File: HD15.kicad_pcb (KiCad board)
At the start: 2 copper layers, 110 x 62 mm, 46 parts, among them CN1 9, CN2 9, CN3 35RAPC4BH3, CN5 B6B-XH-A(LF)(SN), CN6 353180620, J1A JAMMA PINS 3.96MM PITCH 2.2MM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, J1B JAMMA PINS 3.96MM PITCH 2.2MM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, SW1 MJTP1230, SW2 MJTP1230, SW3 DIPSwitch-4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

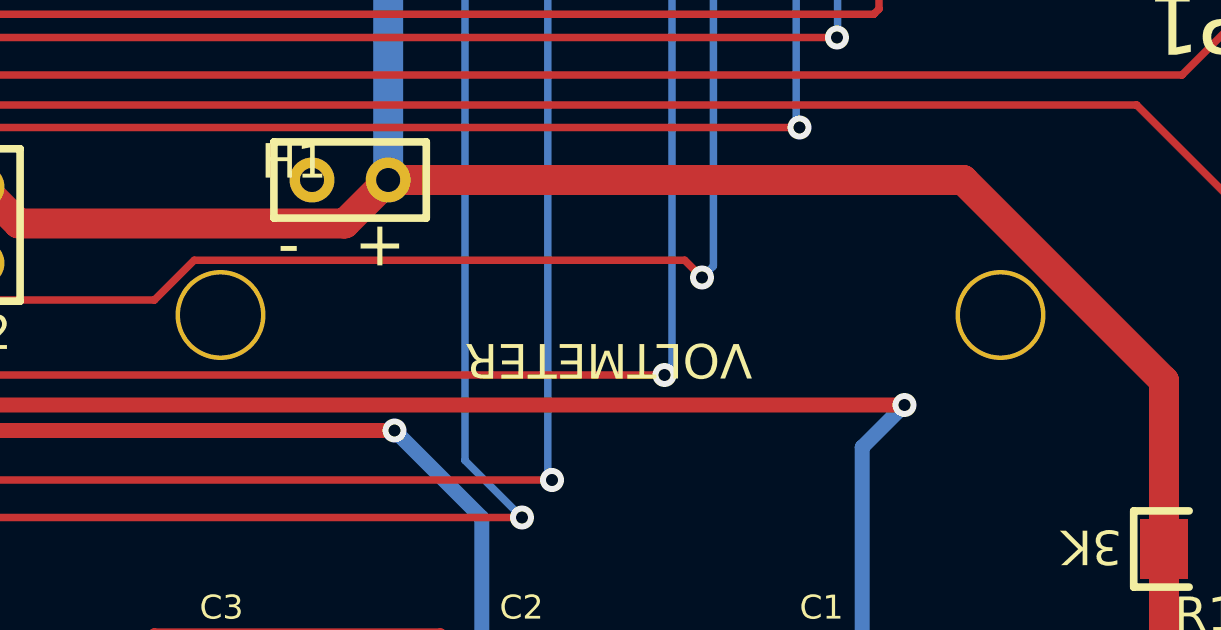
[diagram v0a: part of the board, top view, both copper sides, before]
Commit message: Mounting holes down to 2.0mm
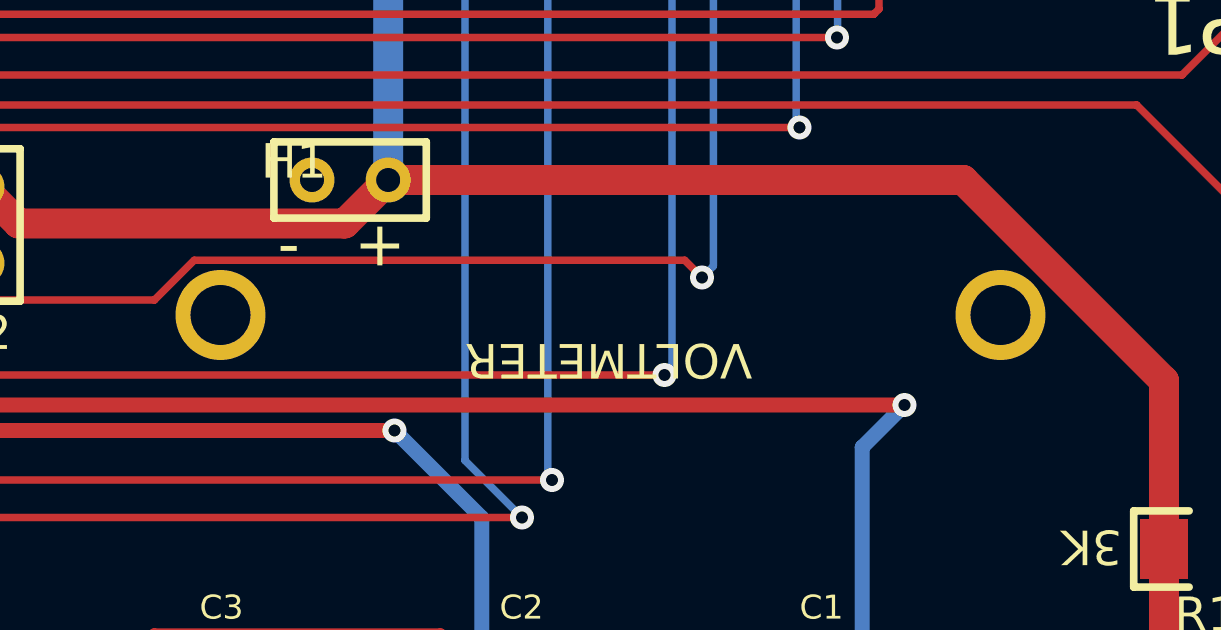
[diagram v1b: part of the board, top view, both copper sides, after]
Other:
- board text added: "REV_2.5+HD15_0.3"
- board text removed: "REV_2.5+HD15_0.2"
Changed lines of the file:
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@@
   )
   (setup
-    (last_trace_width 1)
+    (last_trace_width 0.25)
     (user_trace_width 0.38)
     (user_trace_width 0.5)
@@
     (mod_text_size 1 1)
     (mod_text_width 0.15)
-    (pad_size 1.651 1.651)
-    (pad_drill 1.143)
+    (pad_size 3 3)
+    (pad_drill 2)
     (pad_to_mask_clearance 0)
     (aux_axis_origin 0 0)
@@
       (effects (font (size 1 1) (thickness 0.15)))
     )
-    (pad "" np_thru_hole circle (at -13 0) (size 3 3) (drill 2.7) (layers *.Cu *.Mask))
-    (pad "" np_thru_hole circle (at 13 0) (size 3 3) (drill 2.7) (layers *.Cu *.Mask))
+    (pad "" np_thru_hole circle (at -13 0) (size 3 3) (drill 2) (layers *.Cu *.Mask))
+    (pad "" np_thru_hole circle (at 13 0) (size 3 3) (drill 2) (layers *.Cu *.Mask))
   )
   (module "easyeda:3 PIN HEADER" (layer F.Cu)
@@
     (effects (font (size 1 1) (thickness 0.15)) (justify mirror))
   )
-  (gr_text REV_2.5+HD15_0.2 (at 108.654 29.5) (layer B.SilkS)
+  (gr_text REV_2.5+HD15_0.3 (at 108.654 29.5) (layer B.SilkS)
     (effects (font (size 1.5 1.5) (thickness 0.2)) (justify left mirror))
   )
@@
   (segment (start 51 17) (end 49.799991 15.799991) (width 0.5) (layer B.Cu) (net 4))
   (via (at 49.799991 9.799991) (size 0.8) (drill 0.4) (layers F.Cu B.Cu) (net 4))
-  (segment (start 36.910002 17.25) (end 36.5 17.25) (width 0.5) (layer B.Cu) (net 66))
   (via (at 75.25 -19.5) (size 0.8) (drill 0.4) (layers F.Cu B.Cu) (net 5))
   (segment (start 75.24 -19.49) (end 75.25 -19.5) (width 0.25) (layer B.Cu) (net 5))
@@
   (segment (start 39.4 20.65) (end 39.286411 20.65) (width 0.25) (layer F.Cu) (net 38))
   (segment (start 47.104 20.65) (end 39.4 20.65) (width 0.25) (layer F.Cu) (net 38))
-  (segment (start 19.495012 11.029988) (end 17.025 13.5) (width 0.38) (layer F.Cu) (net 66))
   (segment (start 39.4 20.65) (end 37.9 20.65) (width 0.38) (layer F.Cu) (net 38))
-  (segment (start 27.279988 11.029988) (end 19.495012 11.029988) (width 0.38) (layer F.Cu) (net 66))
   (segment (start 37.9 20.65) (end 36.5 19.25) (width 0.38) (layer F.Cu) (net 38))
   (segment (start 47.104 20.65) (end 37.9 20.65) (width 0.38) (layer F.Cu) (net 38))
@@
   (segment (start 54.1765 21.3) (end 52.895 21.3) (width 0.38) (layer F.Cu) (net 45))
   (segment (start 54.266502 21.209998) (end 54.1765 21.3) (width 0.38) (layer F.Cu) (net 45))
-  (segment (start 29 13.897998) (end 26.712001 11.609999) (width 0.38) (layer F.Cu) (net 64))
-  (segment (start 21.165001 11.609999) (end 17.025 15.75) (width 0.38) (layer F.Cu) (net 64))
-  (segment (start 26.712001 11.609999) (end 21.165001 11.609999) (width 0.38) (layer F.Cu) (net 64))
   (segment (start 39.3 22.2) (end 36.5 25) (width 0.38) (layer F.Cu) (net 46))
-  (segment (start 32.5 17.397998) (end 29 13.897998) (width 0.38) (layer F.Cu) (net 64))
   (segment (start 40.2 21.3) (end 36.5 25) (width 0.38) (layer F.Cu) (net 46))
   (segment (start 47.104 21.3) (end 40.2 21.3) (width 0.38) (layer F.Cu) (net 46))
@@
   (segment (start 6.5 33.25) (end 7.975002 31.774998) (width 0.25) (layer B.Cu) (net 63))
   (segment (start 10.75 32.684315) (end 10.75 33.25) (width 0.25) (layer B.Cu) (net 63))
+  (segment (start 29 13.897998) (end 26.712001 11.609999) (width 0.38) (layer F.Cu) (net 64))
+  (segment (start 21.165001 11.609999) (end 17.025 15.75) (width 0.38) (layer F.Cu) (net 64))
+  (segment (start 26.712001 11.609999) (end 21.165001 11.609999) (width 0.38) (layer F.Cu) (net 64))
+  (segment (start 32.5 17.397998) (end 29 13.897998) (width 0.38) (layer F.Cu) (net 64))
   (segment (start 32.5 19) (end 36.5 23) (width 0.38) (layer F.Cu) (net 64))
   (segment (start 32.5 17.397998) (end 32.5 19) (width 0.38) (layer F.Cu) (net 64))
@@
   (segment (start 36.5 11.5) (end 29.43002 11.5) (width 0.38) (layer F.Cu) (net 65))
   (segment (start 18.24001 10.03499) (end 27.96501 10.03499) (width 0.38) (layer F.Cu) (net 65))
+  (segment (start 36.910002 17.25) (end 36.5 17.25) (width 0.5) (layer B.Cu) (net 66))
+  (segment (start 19.495012 11.029988) (end 17.025 13.5) (width 0.38) (layer F.Cu) (net 66))
+  (segment (start 27.279988 11.029988) (end 19.495012 11.029988) (width 0.38) (layer F.Cu) (net 66))
   (segment (start 33.5 17.25) (end 27.279988 11.029988) (width 0.38) (layer F.Cu) (net 66))
   (segment (start 36.5 17.25) (end 33.5 17.25) (width 0.38) (layer F.Cu) (net 66))

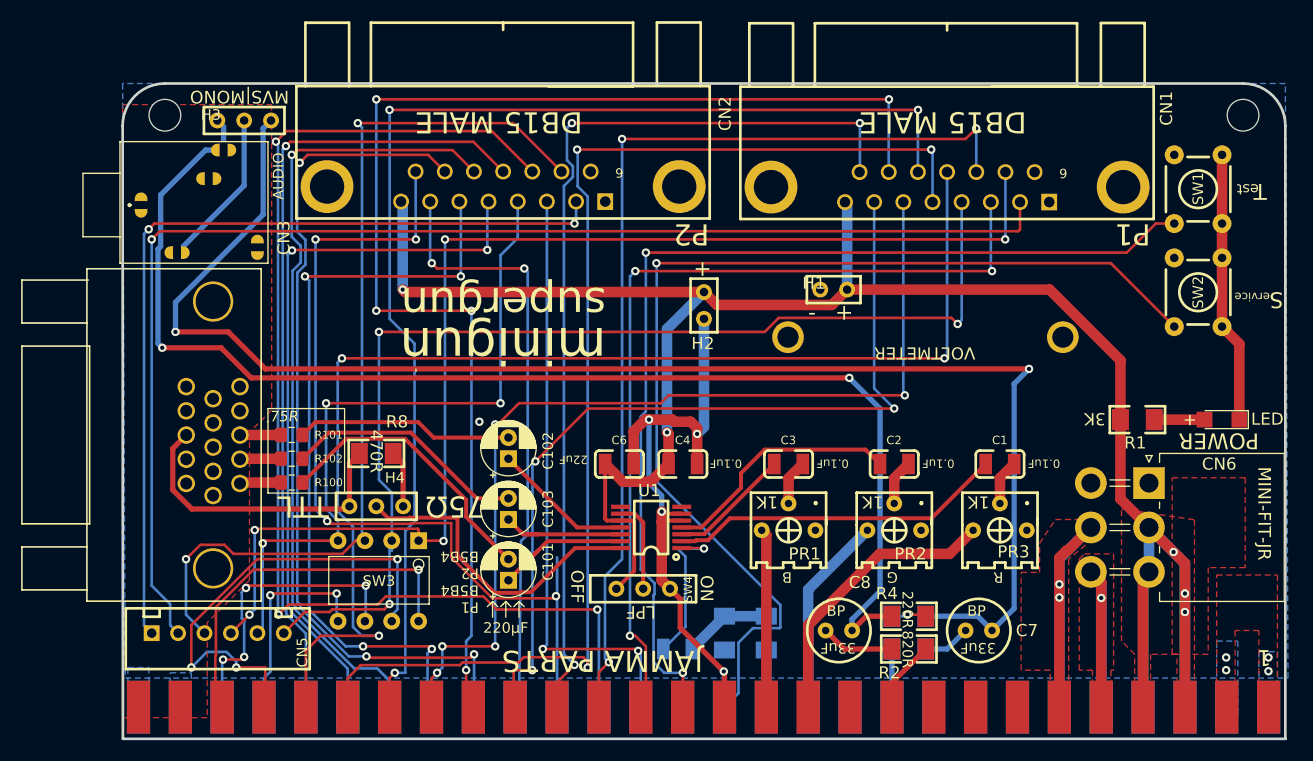
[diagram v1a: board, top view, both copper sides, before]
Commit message: Convert to KiCad 6
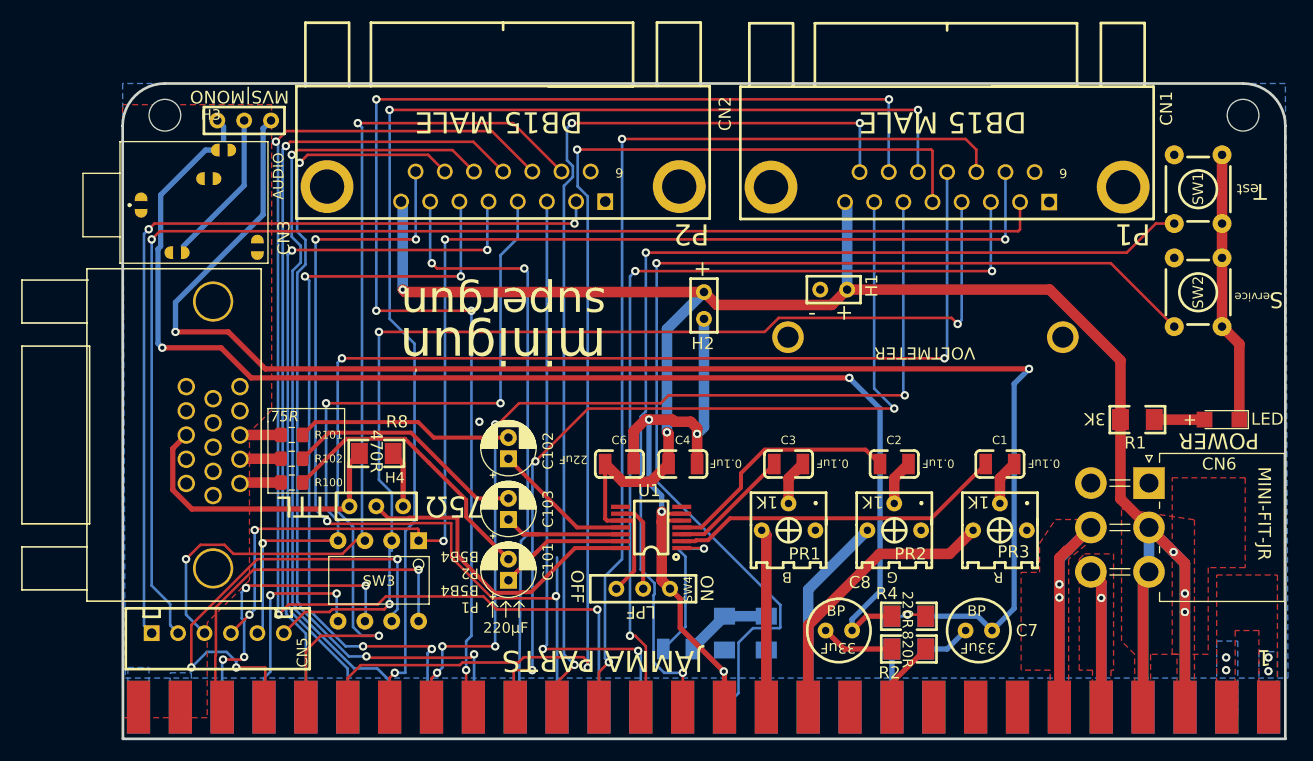
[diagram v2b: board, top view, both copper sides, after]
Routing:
- net P1_START: track 93.0 -> 91.0 mm, vias 3 -> 2
- net P1_B2: vias 3 -> 2
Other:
- net class Default removed

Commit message: Fix 5V pour on obverse
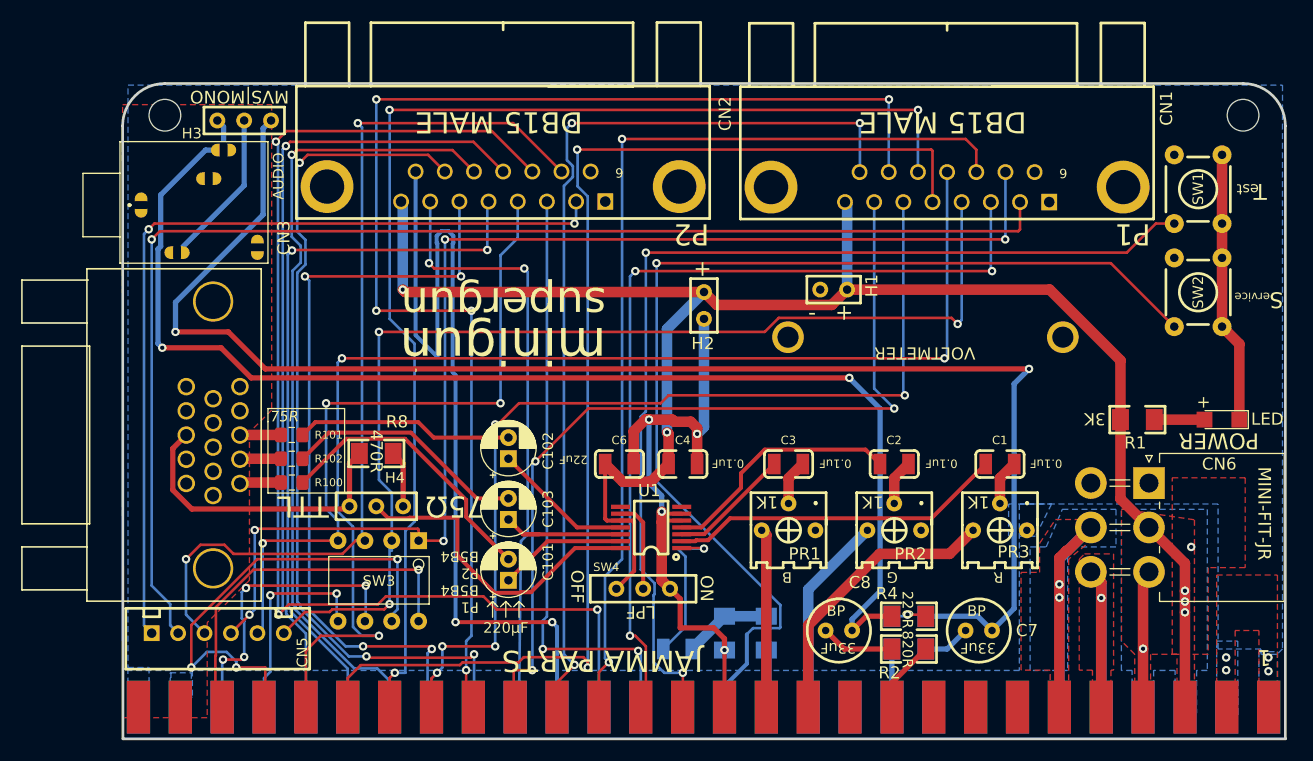
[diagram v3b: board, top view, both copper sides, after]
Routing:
- net +5V: track 213.2 -> 178.0 mm, vias 5 -> 7
- net VIDEO_RED_3: track 16.1 -> 12.1 mm
- net P2_UP: track 83.9 -> 85.9 mm, vias 4 -> 2
- net GND: track 87.6 -> 89.4 mm, vias 10 -> 9
- net VIDEO_SYNC_1: track 9.24 -> 8.34 mm
- added copper zone on B.Cu, net +12V
- added copper zone on B.Cu, net +5V

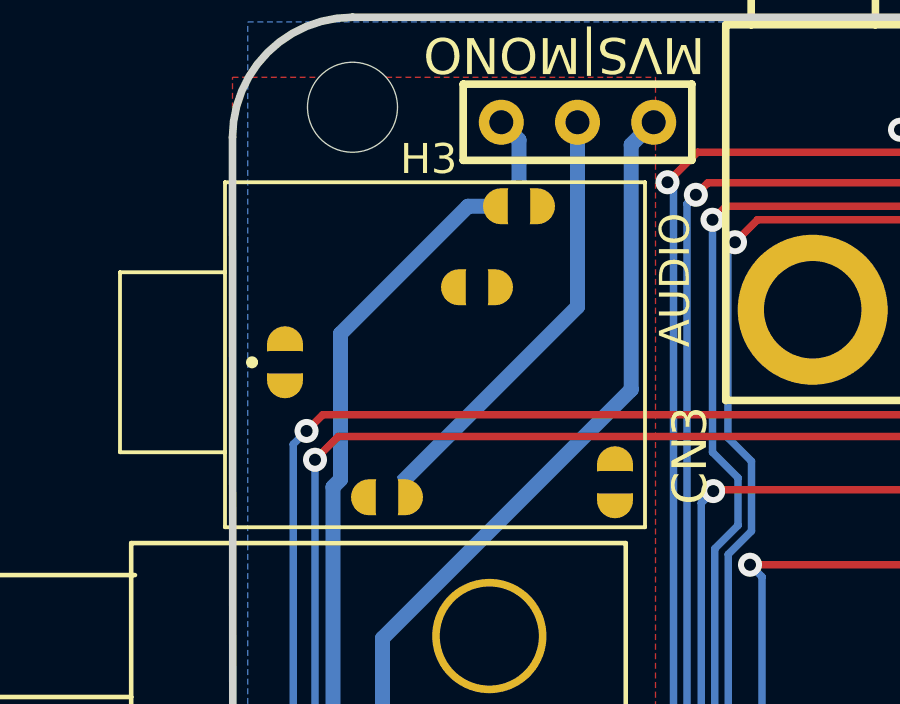
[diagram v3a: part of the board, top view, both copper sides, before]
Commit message: Fix rotated hole in headphone jack
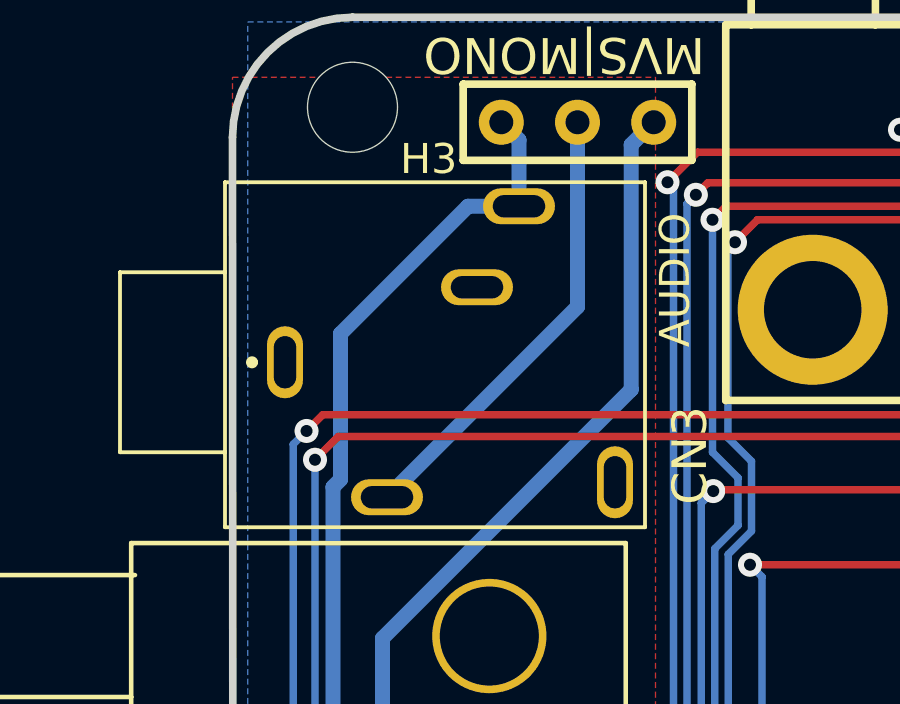
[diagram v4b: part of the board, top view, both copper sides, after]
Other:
- board text added: "HD15 mod by leadedsolder.com v2"
- board text removed: "HD15 mod by leadedsolder.com"
